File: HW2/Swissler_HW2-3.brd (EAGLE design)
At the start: 50 x 50 mm, 22 parts, among them J1 USB-MB-H

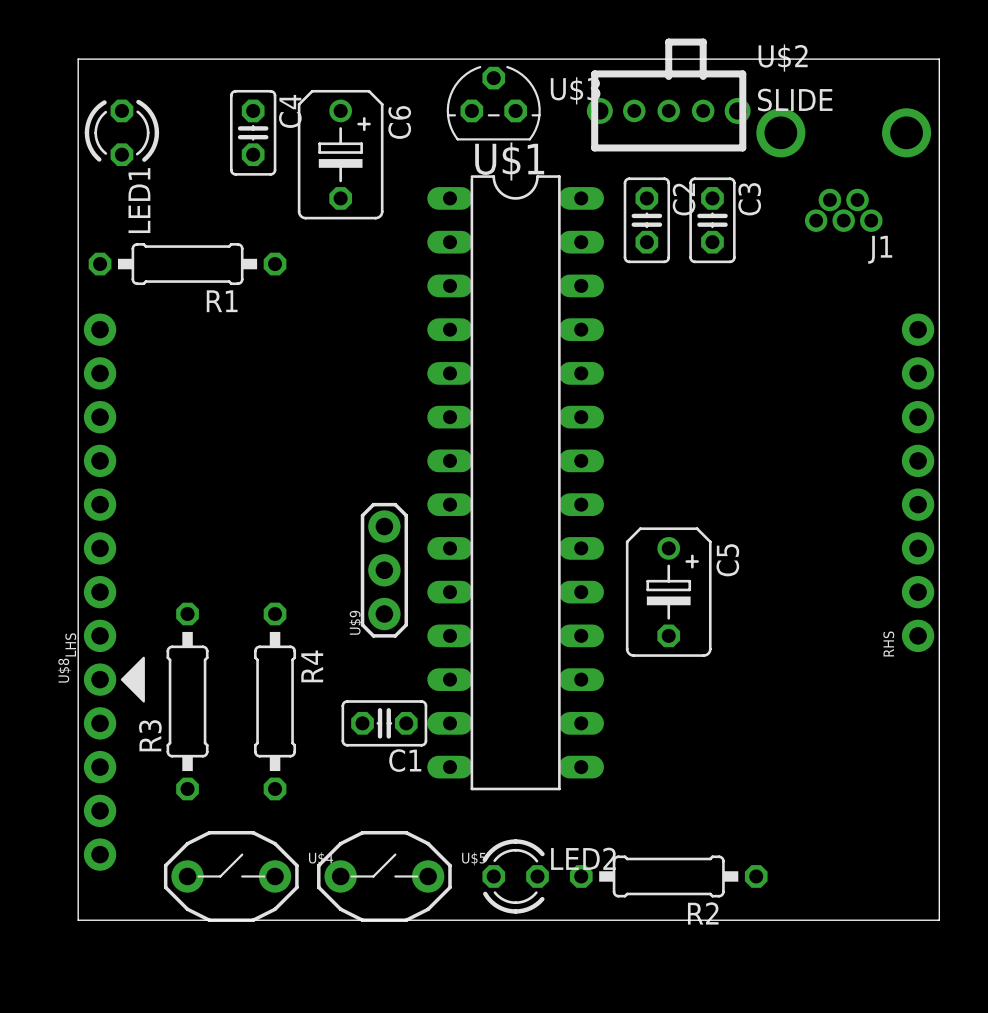
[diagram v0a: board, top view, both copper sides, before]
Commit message: New Routing Approach
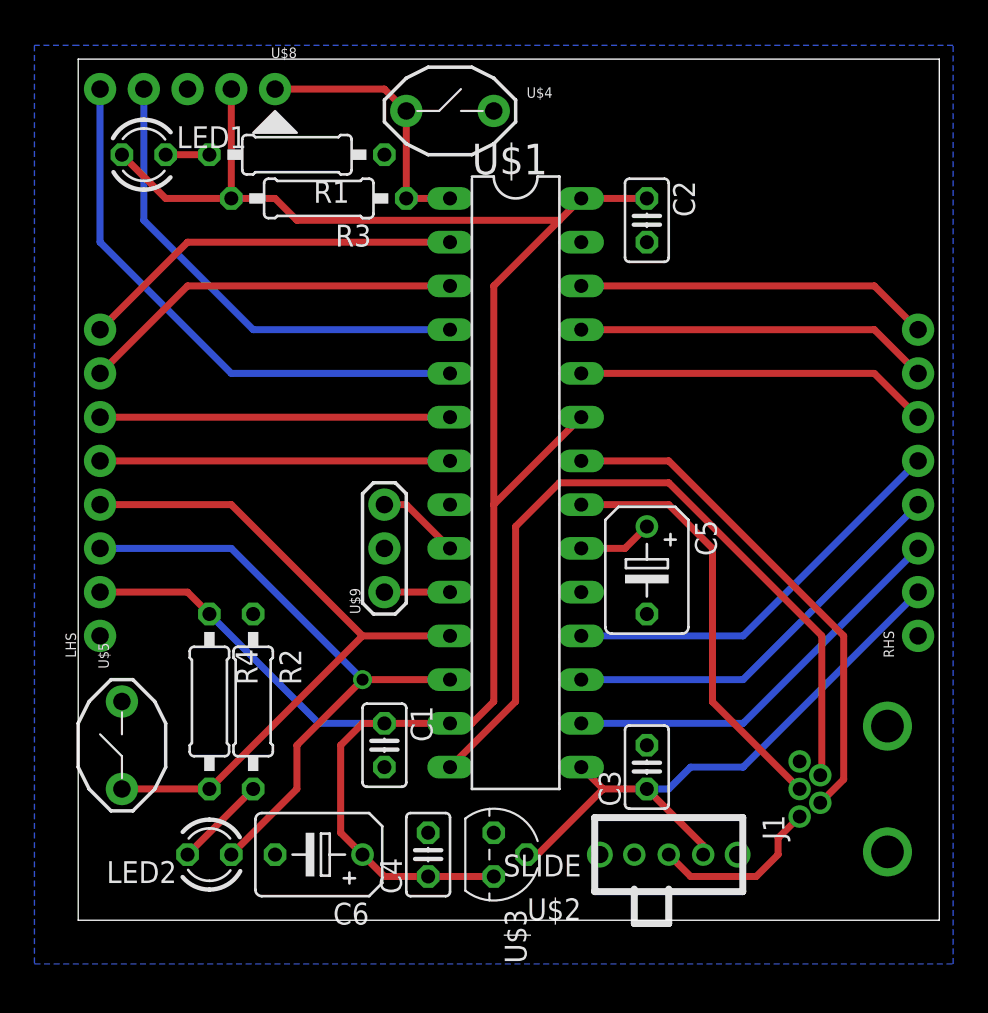
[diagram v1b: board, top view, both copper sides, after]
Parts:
- moved U$4 46.2 mm to (21.6, 47.0)
- moved U$2 43.2 mm to (34.3, 3.81), turned to 180 degrees
- moved U$3 43.2 mm to (24.1, 3.81), turned to 270 degrees
- moved C4 43.1 mm to (20.3, 3.81), turned to 90 degrees
- moved C6 40.7 mm to (14.0, 3.81), turned to 180 degrees
- moved J1 38.2 mm to (47.0, 7.62), turned to 180 degrees
- moved U$8 35.8 mm to (11.4, 48.3), turned to 180 degrees
- moved C3 32.0 mm to (33.0, 8.89), turned to 90 degrees
- moved R3 30.2 mm to (14.0, 41.9), turned to 180 degrees
- moved R2 26.2 mm to (10.2, 12.7), turned to 270 degrees
- moved LED2 17.8 mm to (7.62, 3.81), turned to 180 degrees
- moved U$5 17.0 mm to (2.54, 10.2), turned to 90 degrees
- moved R1 8.98 mm to (12.7, 44.5)
- moved R4 3.81 mm to (7.62, 12.7)
- moved LED1 1.80 mm to (3.81, 44.5), turned to 0 degrees
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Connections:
- net N$1 renamed VBUS
- net N$7 renamed VCAP
- net +5V: now also U$2.1; no longer U$2.3
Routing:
- net +3V3: track 0.00 -> 120.3 mm
- net USBID: track 0.00 -> 46.2 mm
- net B4/USER: track 0.00 -> 41.1 mm
- net A4/LED: track 0.00 -> 36.8 mm, vias 0 -> 1
- net +5V: track 0.00 -> 36.0 mm
- net PGC: track 0.00 -> 32.4 mm
- net D-: track 0.00 -> 29.7 mm
- net PGD: track 0.00 -> 28.0 mm
- net D+: track 0.00 -> 24.7 mm
- net B9: track 0.00 -> 23.8 mm
- net B8: track 0.00 -> 23.8 mm
- net B7: track 0.00 -> 23.8 mm
- net A1: track 0.00 -> 22.4 mm
- net A0: track 0.00 -> 22.4 mm
- net B15: track 0.00 -> 20.6 mm
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- added copper zone on layer 16, net GND

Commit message: Rev3
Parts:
- U$2: value SLIDE -> ON
- moved C3 6.75 mm to (28.6, 3.81), turned to 270 degrees
- moved C2 6.35 mm to (29.2, 45.7), turned to 90 degrees
- moved U$2 1.27 mm to (35.6, 3.81)
- moved C4 0.64 mm to (19.7, 3.81)
- moved U$3 0.63 mm to (23.5, 3.81)
- turned LED2 to 90 degrees
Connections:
- net +5V: now also U$2.3; no longer U$2.1
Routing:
- net A4/LED: track 36.8 -> 42.6 mm, vias 1 -> 0
- net VBUS: track 10.1 -> 7.25 mm
- net +3V3: track 120.3 -> 118.4 mm
- net N$4: track 5.39 -> 3.59 mm
- net +5V: track 36.0 -> 37.1 mm
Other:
- board text added: "+3V3"
- board text added: "+5V"
- board text added: "0"
- board text added: "1"
- board text added: "A0"
- board text added: "A1"
- board text added: "A4"
- board text added: "B13"
- board text added: "B14"
- board text added: "B15"
- board text added: "B2"
- board text added: "B3"
- board text added: "B4"
- board text added: "B7"
- board text added: "B8"
- board text added: "B9"
- board text added: "GND"
